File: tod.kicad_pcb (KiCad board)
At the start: 2 copper layers, 72 x 57 mm, 61 parts, among them J1 Conn_01x04, J2 Conn_01x03, J3 Conn_01x04, J4 Conn_01x03, Q1 BC856, Q2 BC817, Q3 BC856, Q4 BC817, Q5 BC856, Q6 BC817, Q7 BC856, Q8 BC817, U1 PC817, U2 PC817, U3 PC817, U4 PC817

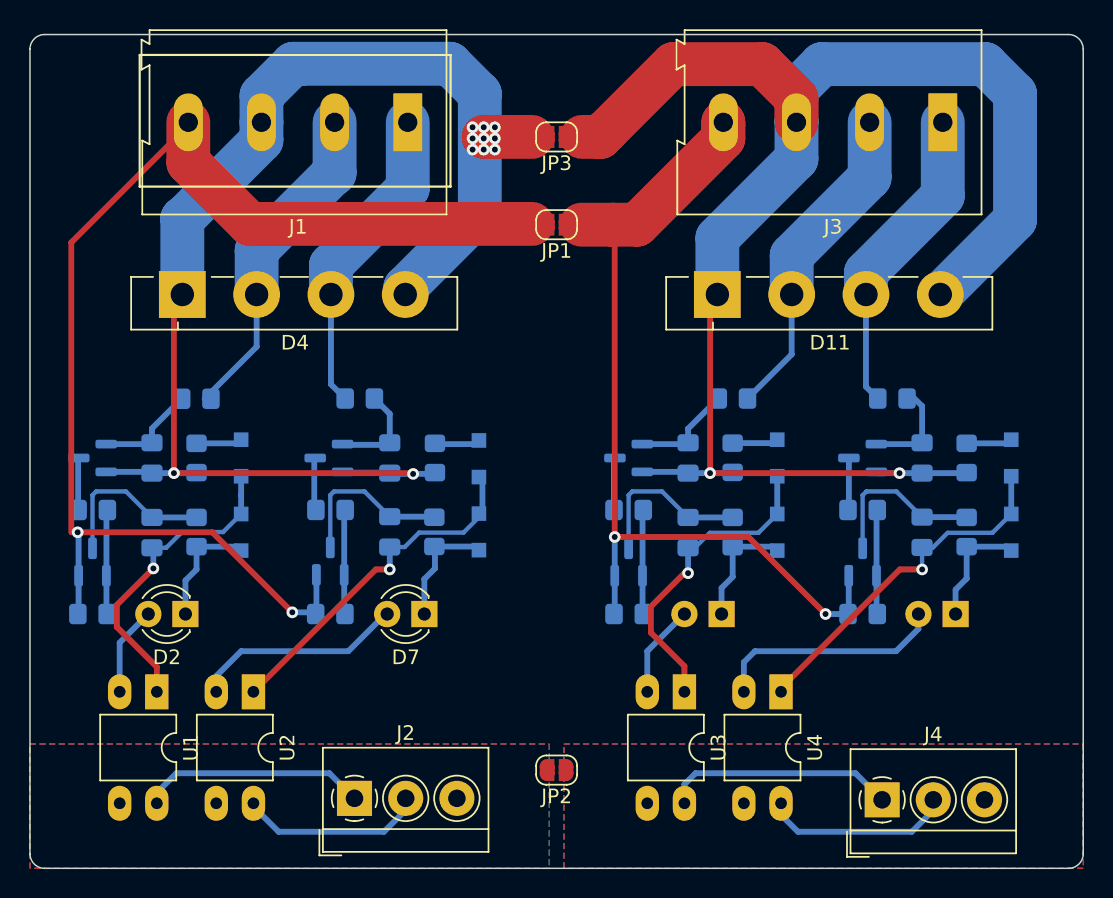
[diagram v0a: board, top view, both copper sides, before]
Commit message: Tweak silkscreen.
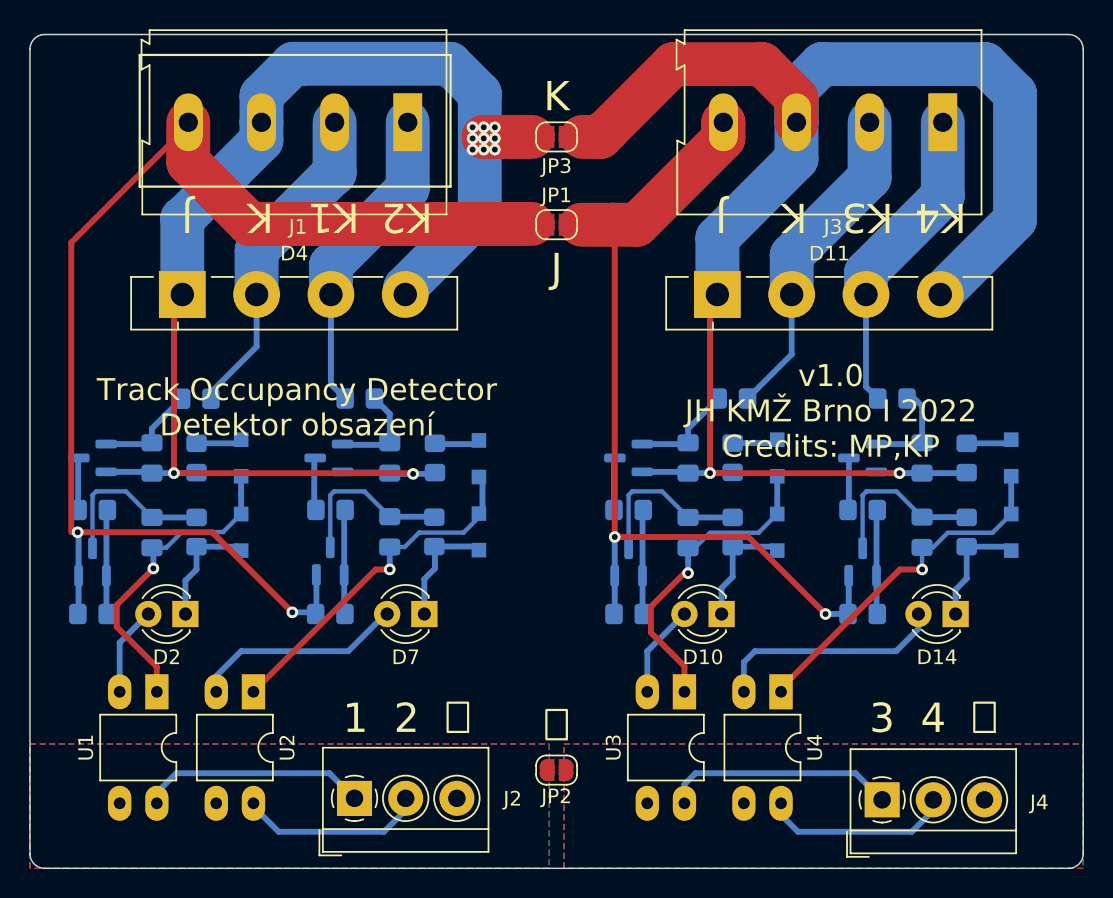
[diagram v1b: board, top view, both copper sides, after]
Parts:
- D10, D14: moved to F.Cu
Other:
- board text added: "1"
- board text added: "2"
- board text added: "3"
- board text added: "4"
- board text added: "J"
- board text added: "K"
- board text added: "K1"
- board text added: "K2"
- board text added: "K3"
- board text added: "K4"
- board text added: "Track Occupancy Detector Detektor obsazení"
- board text added: "v1.0 JH KMŽ Brno I 2022 Credits: MP,KP"
- board text added: "⏚"

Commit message: Add proper MVE252-5-V footprints.
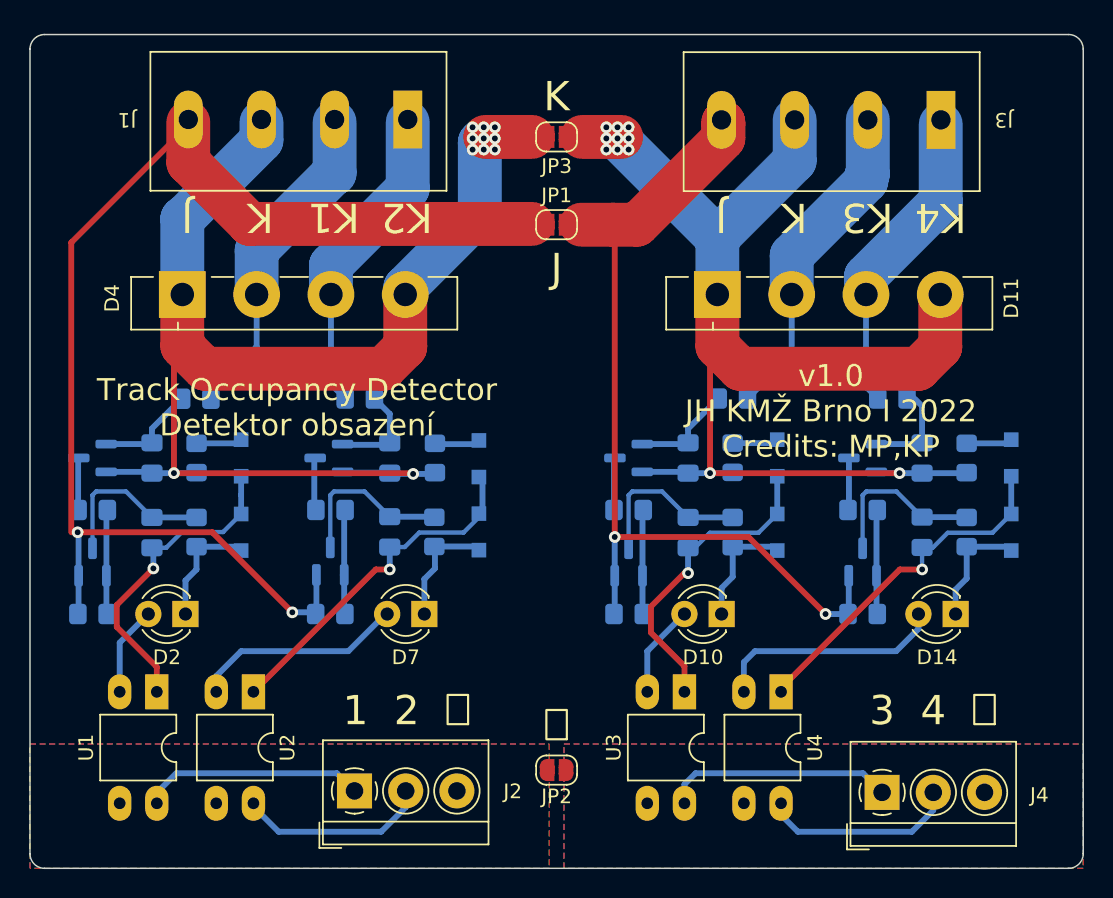
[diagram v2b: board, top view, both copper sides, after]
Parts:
- J1, J3: footprint TerminalBlock:TerminalBlock_Altech_AK300-4_P5.00mm -> TerminalBlock_Euroclamp:MVE252-5-V-2x
- Q1, Q3: value BC856 -> BC856B
- moved J3 7.53 mm to (167.9, 68.6)
- moved J1 7.40 mm to (131.4, 68.6)
- moved J2 0.51 mm to (135.2, 114.7)
- moved J4 0.51 mm to (171.3, 114.8)
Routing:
- net /K2: track 105.9 -> 90.3 mm, vias 2 -> 11
- net /T2: track 12.8 -> 13.7 mm
- net /K1: track 93.5 -> 93.0 mm
- net /T4: track 13.0 -> 13.5 mm

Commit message: Add mountholes.
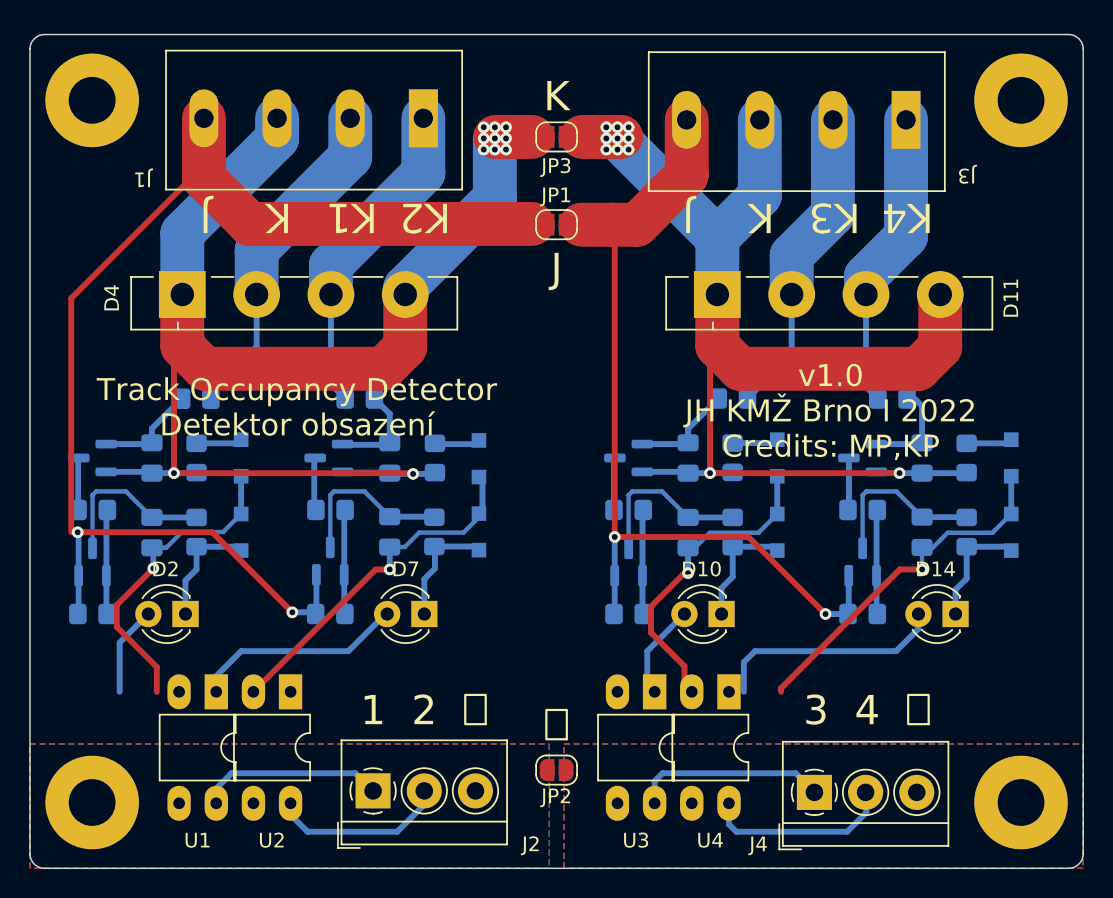
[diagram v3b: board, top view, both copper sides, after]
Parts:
- added H1: MountingHole, MountingHole:MountingHole_3.2mm_M3_Pad, F.Cu at (117.2, 115.5)
- added H2: MountingHole, MountingHole:MountingHole_3.2mm_M3_Pad, F.Cu at (180.8, 67.5)
- added H3: MountingHole, MountingHole:MountingHole_3.2mm_M3_Pad, F.Cu at (117.2, 67.5)
- added H4: MountingHole, MountingHole:MountingHole_3.2mm_M3_Pad, F.Cu at (180.8, 115.5)
- moved J4 4.63 mm to (166.6, 114.8)
- moved U1 4.06 mm to (125.7, 107.9)
- moved U4 3.56 mm to (160.8, 107.9)
- moved U2 2.54 mm to (130.8, 107.9)
- moved J3 2.38 mm to (165.5, 68.6)
- moved U3 2.04 mm to (155.7, 107.9)
- moved J2 1.27 mm to (136.5, 114.7)
- moved J1 1.07 mm to (132.5, 68.5)
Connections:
- U4 pad 3: /GNDB -> /T4
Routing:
- net /T1: track 15.3 -> 12.7 mm
- net /T3: track 15.7 -> 13.2 mm
- net /T2: track 13.7 -> 12.1 mm
- net /J2: track 60.9 -> 59.8 mm
- net /K2A: track 22.5 -> 21.5 mm
- net /K2: track 90.3 -> 89.3 mm
- net /K1B: track 20.3 -> 21.0 mm
- net /K2B: track 21.2 -> 20.5 mm
- net /K1A: track 22.7 -> 23.3 mm
- net /T4: track 13.5 -> 13.0 mm

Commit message: Add JLCPCB_CORRECTION where required.
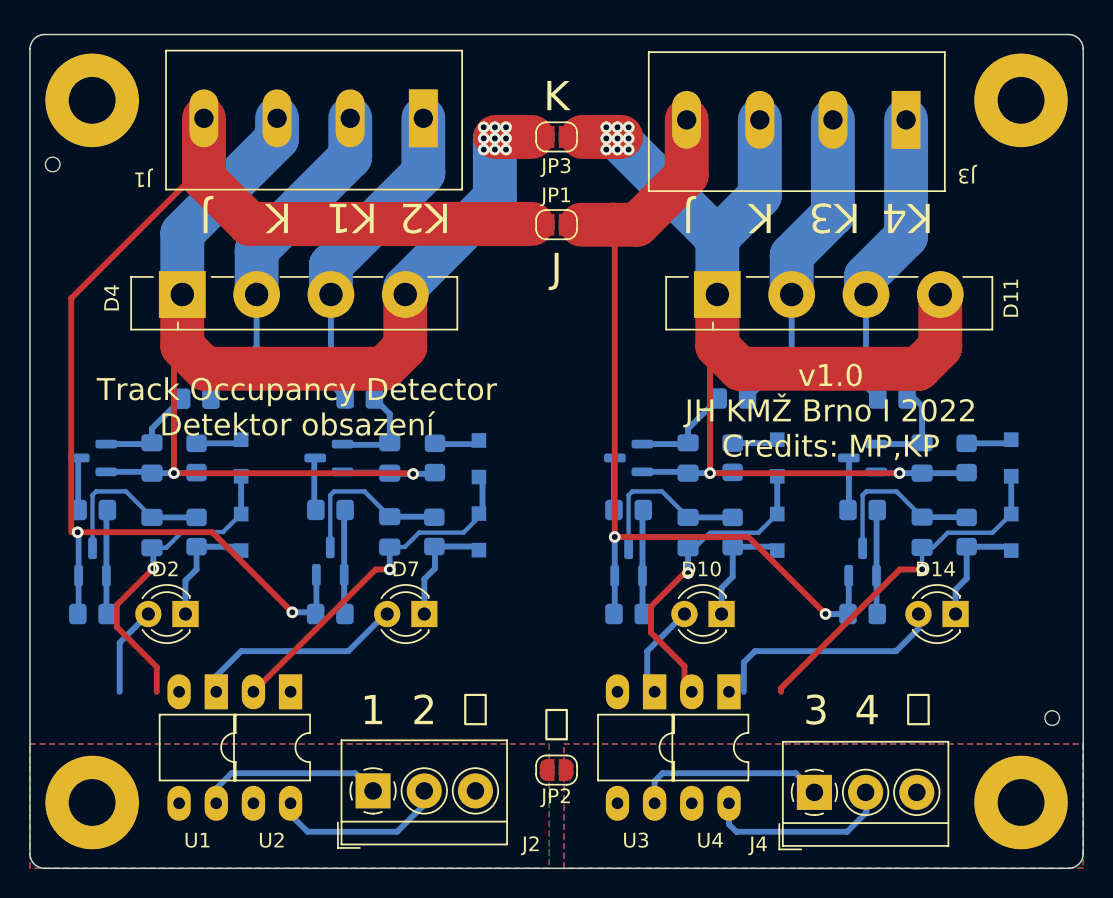
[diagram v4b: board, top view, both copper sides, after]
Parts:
- added REF**: NPTH, kikit:NPTH, F.Cu at (114.6, 71.9)
- added REF**: NPTH, kikit:NPTH, F.Cu at (182.9, 109.7)
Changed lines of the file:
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@@
     )
+  )
+  (footprint "kikit:NPTH" (layer "F.Cu")
+    (at 114.554 71.882)
+    (attr through_hole)
+    (fp_text reference "REF**" (at 0 0.5) (layer "F.SilkS") hide
+      (effects (font (size 1 1) (thickness 0.15)))
+    )
+    (fp_text value "NPTH" (at 0 -0.5) (layer "F.Fab") hide
+      (effects (font (size 1 1) (thickness 0.15)))
+    )
+    (pad "" np_thru_hole circle locked (at 0 0) (size 1 1) (drill 1) (layers *.Cu *.Mask))
   )
   (footprint "TerminalBlock_Euroclamp:MVE252-5-V-2x" (layer "F.Cu")
@@
     (pad "1" thru_hole circle (at 0 0) (size 6.4 6.4) (drill 3.2) (layers *.Cu *.Mask))
   )
+  (footprint "kikit:NPTH" (layer "F.Cu")
+    (at 182.88 109.728)
+    (attr through_hole)
+    (fp_text reference "REF**" (at 0 0.5) (layer "F.SilkS") hide
+      (effects (font (size 1 1) (thickness 0.15)))
+    )
+    (fp_text value "NPTH" (at 0 -0.5) (layer "F.Fab") hide
+      (effects (font (size 1 1) (thickness 0.15)))
+    )
+    (pad "" np_thru_hole circle locked (at 0 0) (size 1 1) (drill 1) (layers *.Cu *.Mask))
+  )
   (footprint "TerminalBlock_4Ucon:TerminalBlock_4Ucon_1x03_P3.50mm_Horizontal" (layer "F.Cu")

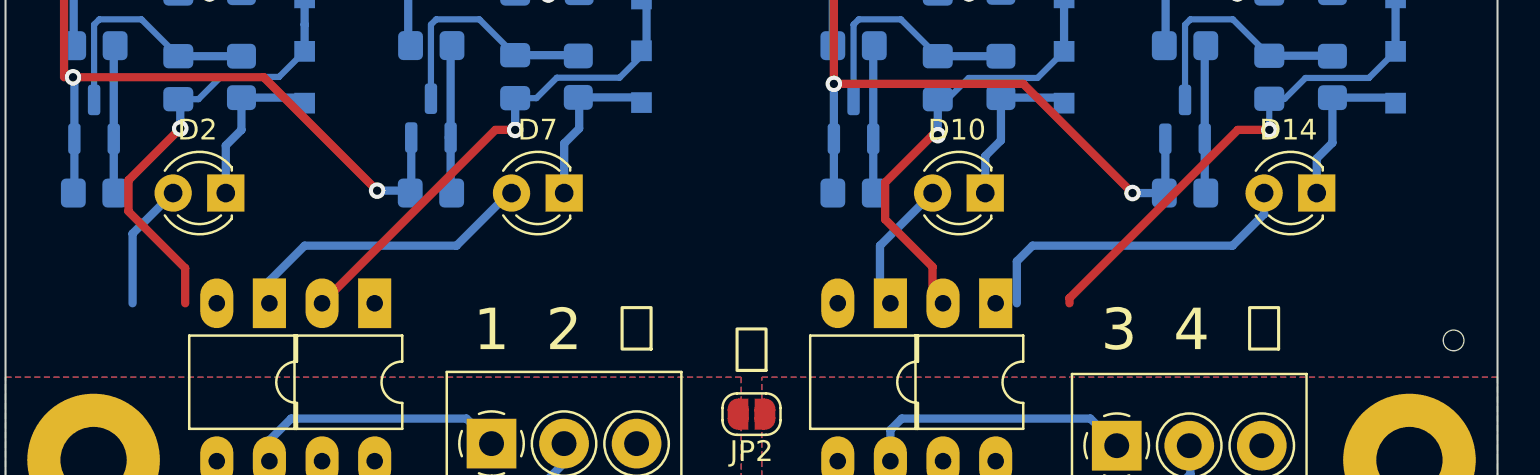
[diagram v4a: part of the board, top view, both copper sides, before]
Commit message: Wire unrouted paths.
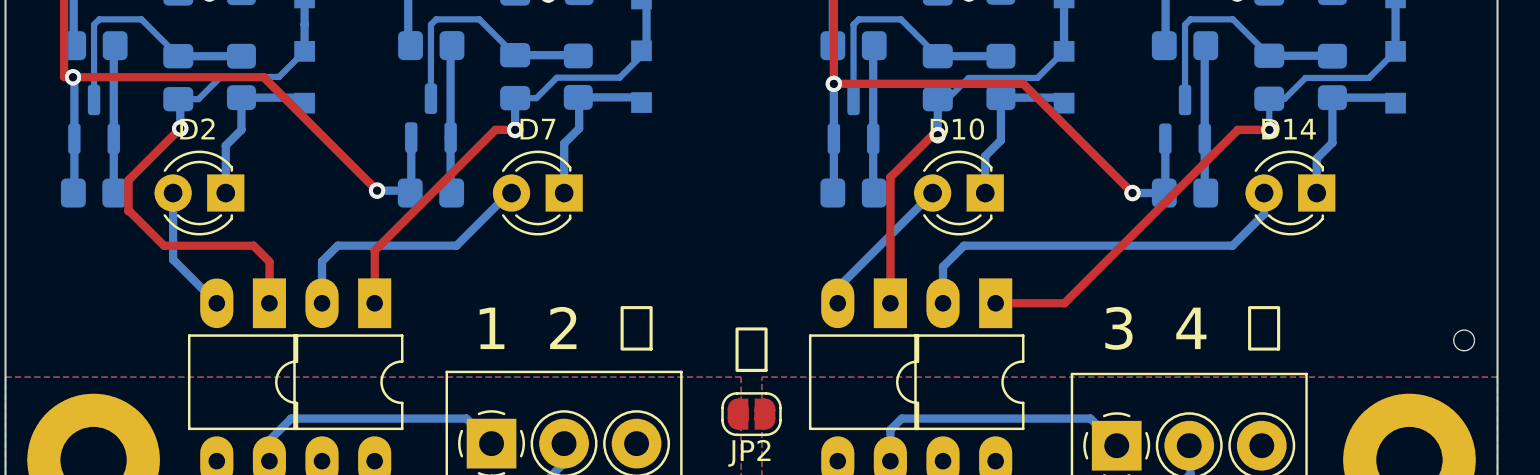
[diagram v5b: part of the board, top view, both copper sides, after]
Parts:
- moved REF** 0.51 mm to (183.4, 109.7)
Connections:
- U4 pad 3: /T4 -> /GNDB
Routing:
- net Net-(C2-Pad1): track 21.7 -> 25.9 mm
- net Net-(C8-Pad1): track 24.4 -> 27.8 mm
- net Net-(D14-Pad2): track 15.9 -> 19.3 mm
- net Net-(D7-Pad2): track 14.6 -> 12.6 mm
- net Net-(C6-Pad1): track 21.6 -> 20.6 mm
- net Net-(C4-Pad1): track 24.3 -> 23.2 mm
- net Net-(D10-Pad2): track 6.37 -> 7.21 mm
